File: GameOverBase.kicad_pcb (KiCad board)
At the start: 4 copper layers, 50 x 30 mm, 49 parts, among them J1 USB_C_DEALON-USB-US31-106, J2 Serial Port, J3 add-on conn, Q1 PMN48XP, SW1 SW_DIP_x08, SW2 boot, SW3 Reset, U1 ESP32-WROOM-E, U2 4021, U3 MCP73831-2ACI-OT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

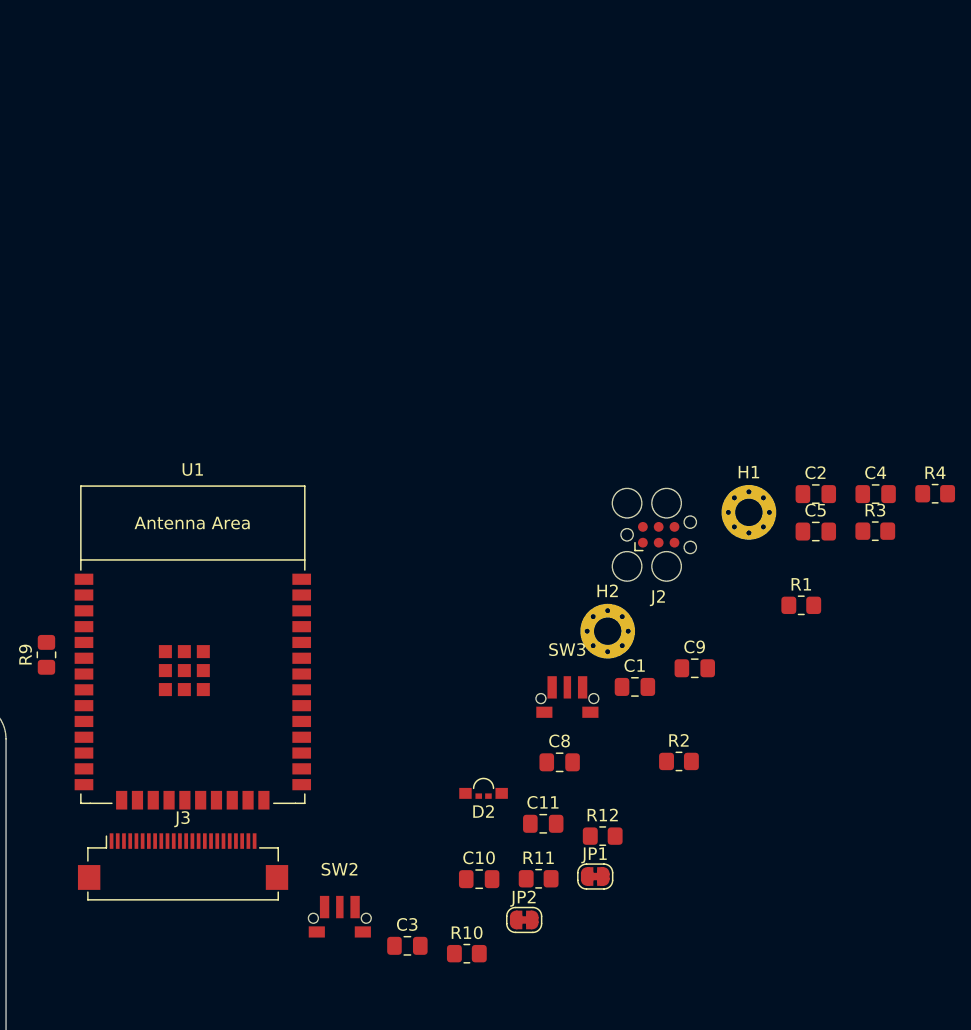
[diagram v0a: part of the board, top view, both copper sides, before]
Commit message: Groups ESP32 circuitry and add-on connector
To do this, I reorganized the order the GPIO pins are broken out to the
add-on connector.

This is still missing the decoupling capacitors on the connector
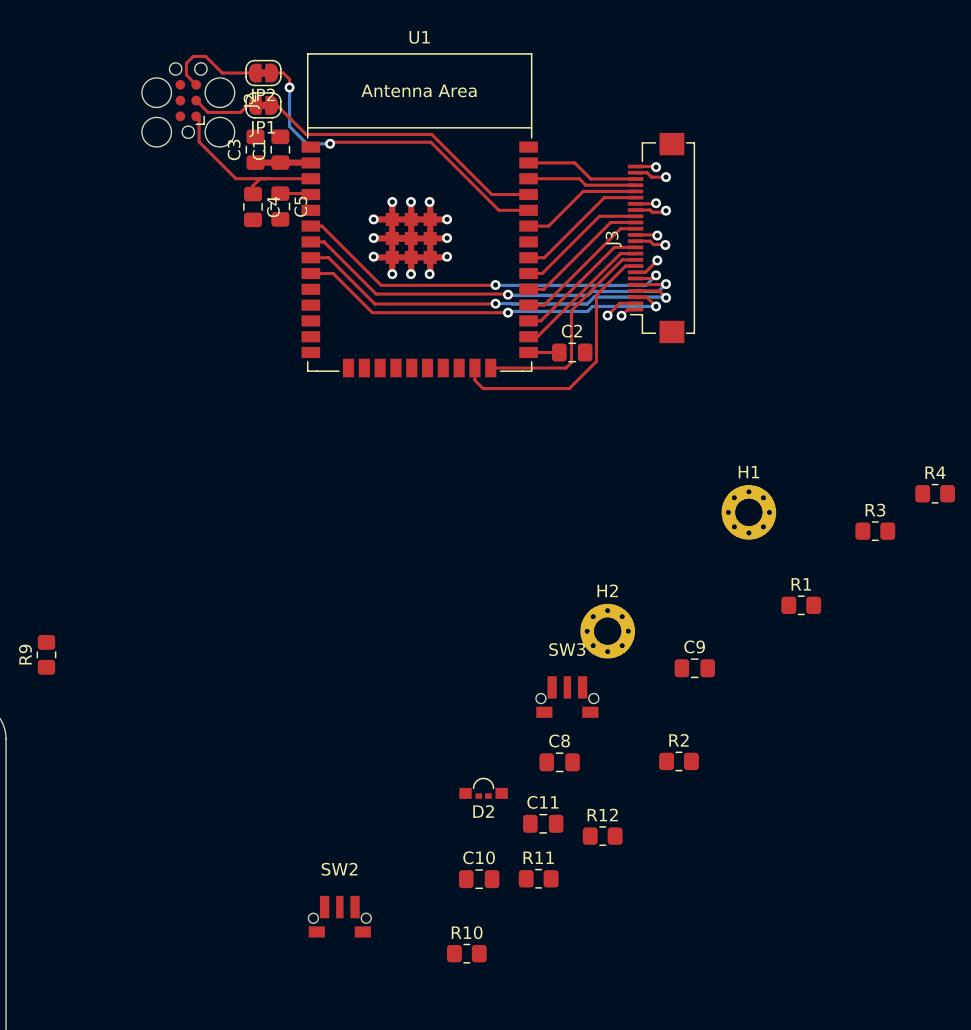
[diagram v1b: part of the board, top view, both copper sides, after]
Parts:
- moved JP2 71.2 mm to (190.7, 29.5), turned to 180 degrees
- moved JP1 67.5 mm to (190.7, 32.1), turned to 180 degrees
- moved C3 65.1 mm to (190.1, 35.6), turned to 90 degrees
- moved J3 63.2 mm to (222.4, 42.8), turned to 90 degrees
- moved C4 55.1 mm to (189.8, 40.2), turned to -90 degrees
- moved C1 51.7 mm to (192.1, 35.6), turned to 90 degrees
- moved J2 51.5 mm to (184.7, 31.7), turned to 90 degrees
- moved C5 50.3 mm to (192.1, 40.2), turned to -90 degrees
- moved U1 39.2 mm to (203.2, 42.5)
- moved C2 22.6 mm to (215.5, 52.0)
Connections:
- J3 pad 10: IO18 -> IO4
- J3 pad 11: IO19 -> IO16
- J3 pad 14: IO21 -> IO17
- J3 pad 15: IO22 -> IO5
- J3 pad 16: IO23 -> IO18
- J3 pad 19: IO32 -> IO19
- J3 pad 20: IO33 -> IO21
- J3 pad 21: IO34 -> IO22
- J3 pad 22: IO35 -> IO23
- J3 pad 3: IO2 -> IO33
- J3 pad 4: IO4 -> IO32
- J3 pad 5: IO5 -> IO35
- J3 pad 6: IO15 -> IO34
- J3 pad 8: IO16 -> IO15
- J3 pad 9: IO17 -> IO2
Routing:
- net GND: track 0.00 -> 46.7 mm, vias 0 -> 17
- net IO35: track 0.00 -> 33.2 mm, vias 0 -> 2
- net IO32: track 0.00 -> 33.1 mm, vias 0 -> 2
- net IO34: track 0.00 -> 31.8 mm, vias 0 -> 2
- net IO33: track 0.00 -> 31.2 mm, vias 0 -> 2
- net ESP_RX: track 0.00 -> 27.6 mm, vias 0 -> 2
- net ESP_TX: track 0.00 -> 23.6 mm
- net IO15: track 0.00 -> 21.4 mm
- net IO2: track 0.00 -> 17.7 mm
- net ESP_EN: track 0.00 -> 14.2 mm
- net +3V3: track 0.00 -> 13.5 mm, vias 0 -> 4
- net IO4: track 0.00 -> 11.4 mm
- net IO17: track 0.00 -> 11.1 mm
- net IO16: track 0.00 -> 11.0 mm
- net IO5: track 0.00 -> 10.8 mm
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
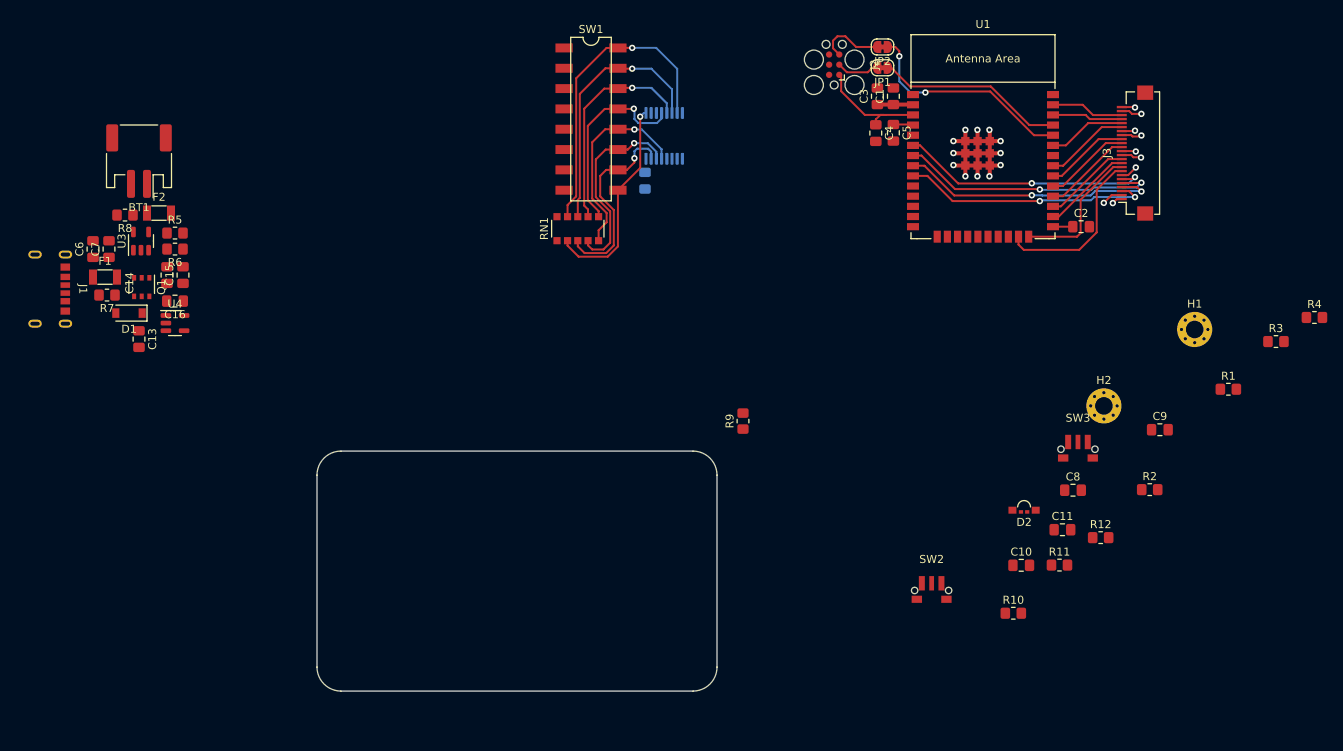
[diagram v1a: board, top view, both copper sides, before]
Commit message: Adds decoupling caps to the add-on connector and places the ESP on the pcb
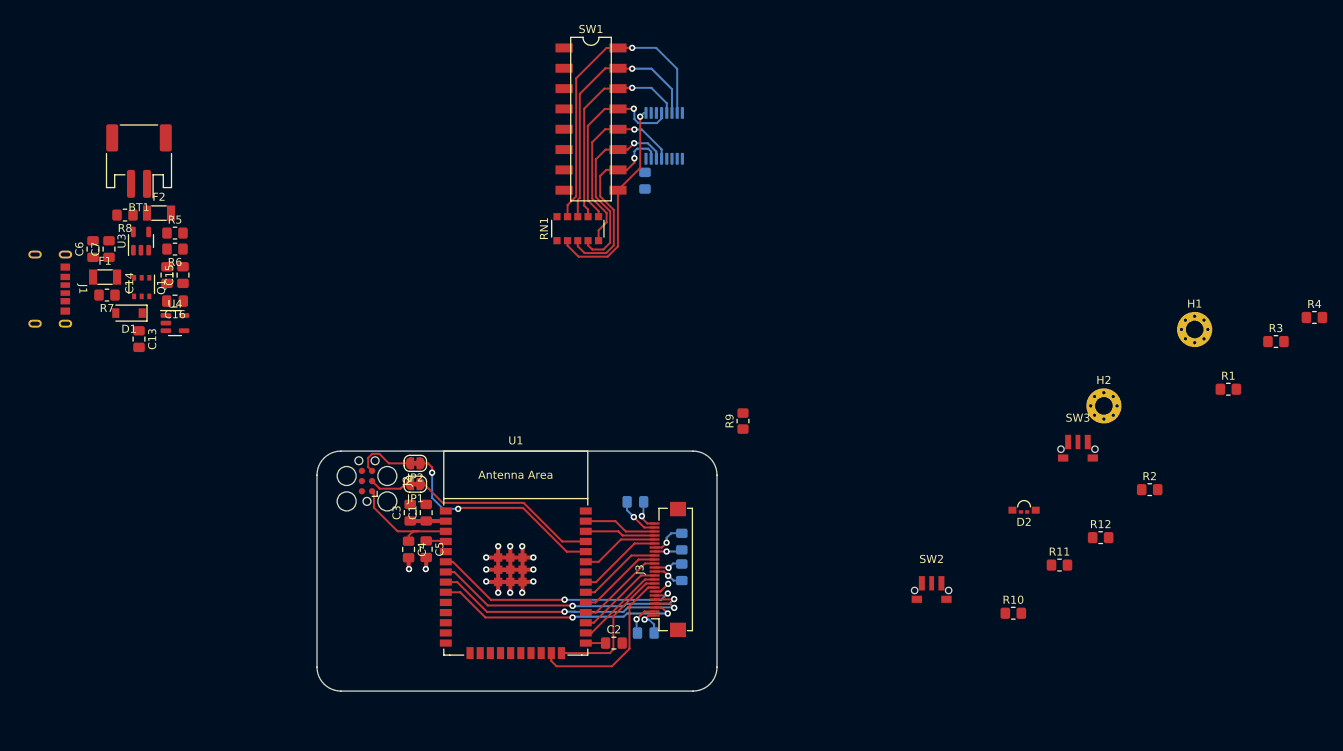
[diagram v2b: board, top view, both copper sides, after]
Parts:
- C10, C11, C8, C9: moved to B.Cu
- moved C1 78.2 mm to (133.7, 87.7)
- moved C3 78.2 mm to (131.7, 87.7)
- moved C4 78.2 mm to (131.4, 92.3)
- moved C5 78.2 mm to (133.7, 92.3)
- moved J2 78.2 mm to (126.2, 83.8)
- moved JP1 78.2 mm to (132.3, 84.1)
- moved JP2 78.2 mm to (132.3, 81.5)
- moved U1 78.2 mm to (144.8, 94.5)
- moved C2 78.2 mm to (157.1, 104.0)
- moved J3 78.2 mm to (164.1, 94.8)
- moved C9 69.1 mm to (161.1, 102.8), turned to 180 degrees
- moved C11 53.5 mm to (159.8, 86.3)
- moved C8 49.3 mm to (165.6, 91.3), turned to 90 degrees
- moved C10 42.4 mm to (165.6, 95.2), turned to 90 degrees
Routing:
- net GND: track 46.7 -> 58.3 mm, vias 17 -> 19
- net +3V3: track 13.5 -> 21.2 mm
- net Net-(J2-Pin_5): track 8.37 -> 7.78 mm

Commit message: Roughly routes buttons and RGB led
To make this routing better I also switched around the GPIO pins for the
RGB leds.
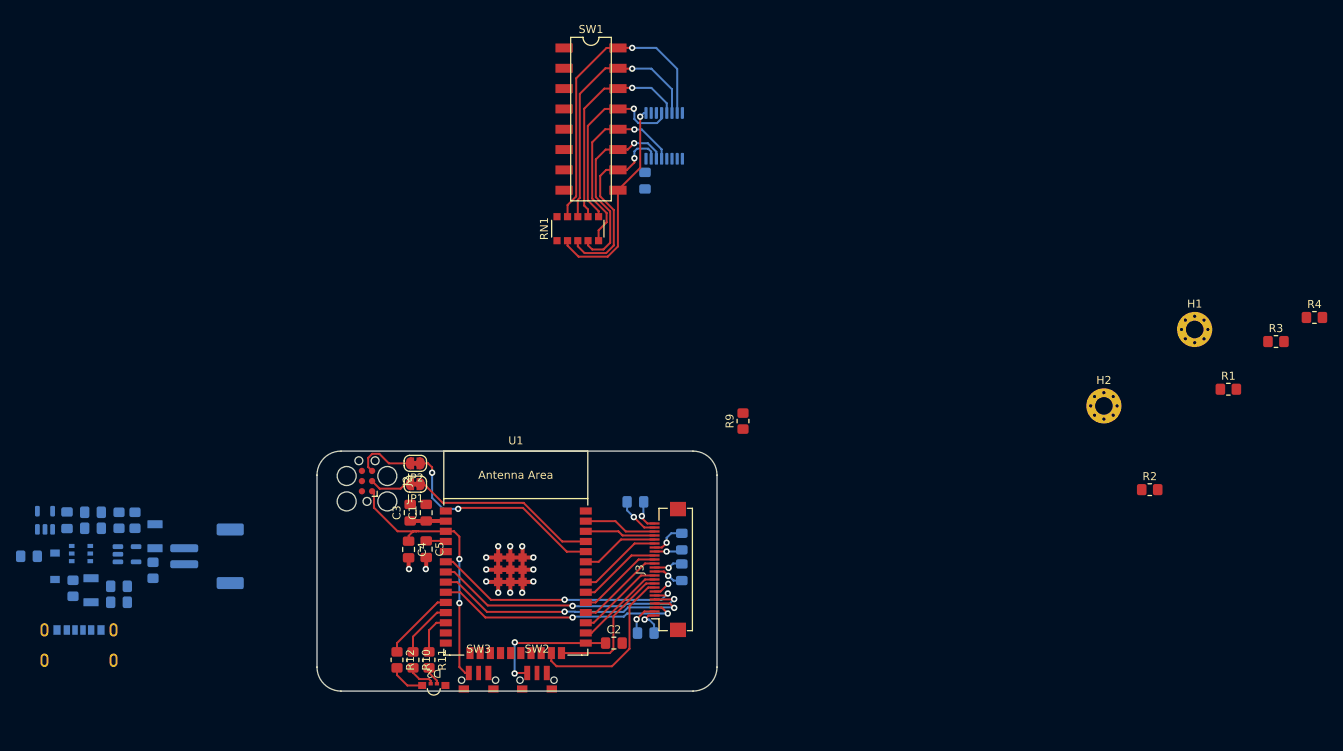
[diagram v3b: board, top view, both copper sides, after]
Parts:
- BT1, C13, C14, C15, C16, C6, C7, D1, F1, F2, J1, Q1, R5, R6, R7, R8, U3, U4: moved to B.Cu
- moved R12 89.3 mm to (130.0, 106.1), turned to -90 degrees
- moved SW3 80.3 mm to (140.2, 107.7)
- moved R11 79.7 mm to (134.0, 106.1), turned to -90 degrees
- moved D2 77.0 mm to (134.6, 109.3), turned to 180 degrees
- moved R10 75.3 mm to (132.0, 106.1), turned to -90 degrees
- moved SW2 50.6 mm to (147.5, 107.7)
- moved BT1 50.1 mm to (106.2, 93.2), turned to -90 degrees
- moved J1 45.6 mm to (90.2, 105.2), turned to 180 degrees
- moved R8 44.5 mm to (99.5, 94.9), turned to -90 degrees
- moved C6 44.3 mm to (95.2, 98.9), turned to 0 degrees
- moved C7 42.2 mm to (95.2, 96.9), turned to 0 degrees
- moved F2 40.4 mm to (99.8, 90.7), turned to 90 degrees
- moved F1 39.2 mm to (91.8, 97.4), turned to 90 degrees
- moved U3 39.2 mm to (96.2, 92.9), turned to 0 degrees
- moved R7 36.9 mm to (89.5, 97.2), turned to -90 degrees
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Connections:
- U1 pad 10: BAT_IND_R -> BAT_IND_B
- U1 pad 11: BAT_IND_G -> BAT_IND_R
- U1 pad 12: BAT_IND_B -> BAT_IND_G
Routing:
- net ESP_EN: track 14.2 -> 34.0 mm, vias 0 -> 2
- net ESP_BOOT: track 2.47 -> 16.9 mm, vias 0 -> 2
- net BAT_IND_B: track 0.00 -> 9.30 mm
- net BAT_IND_R: track 0.00 -> 7.25 mm
- net BAT_IND_G: track 0.00 -> 5.19 mm
- net Net-(D2-BK): track 0.00 -> 4.58 mm
- net Net-(D2-RK): track 0.00 -> 3.60 mm
- net Net-(D2-GK): track 0.00 -> 2.39 mm

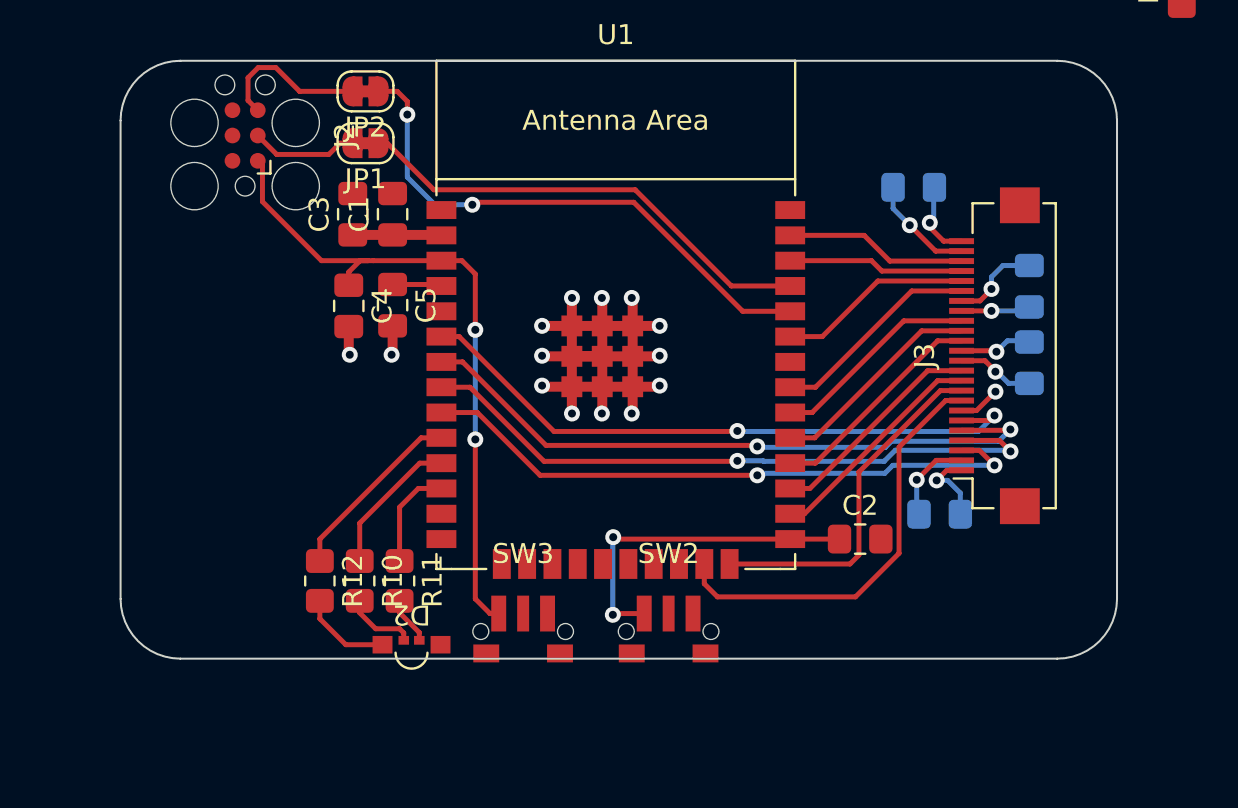
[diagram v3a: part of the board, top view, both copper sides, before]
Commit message: Increases board height to 3.5cm
This increases the overall size quite a bit, but gives us much more
space, which will be necessary for the DIP switches.
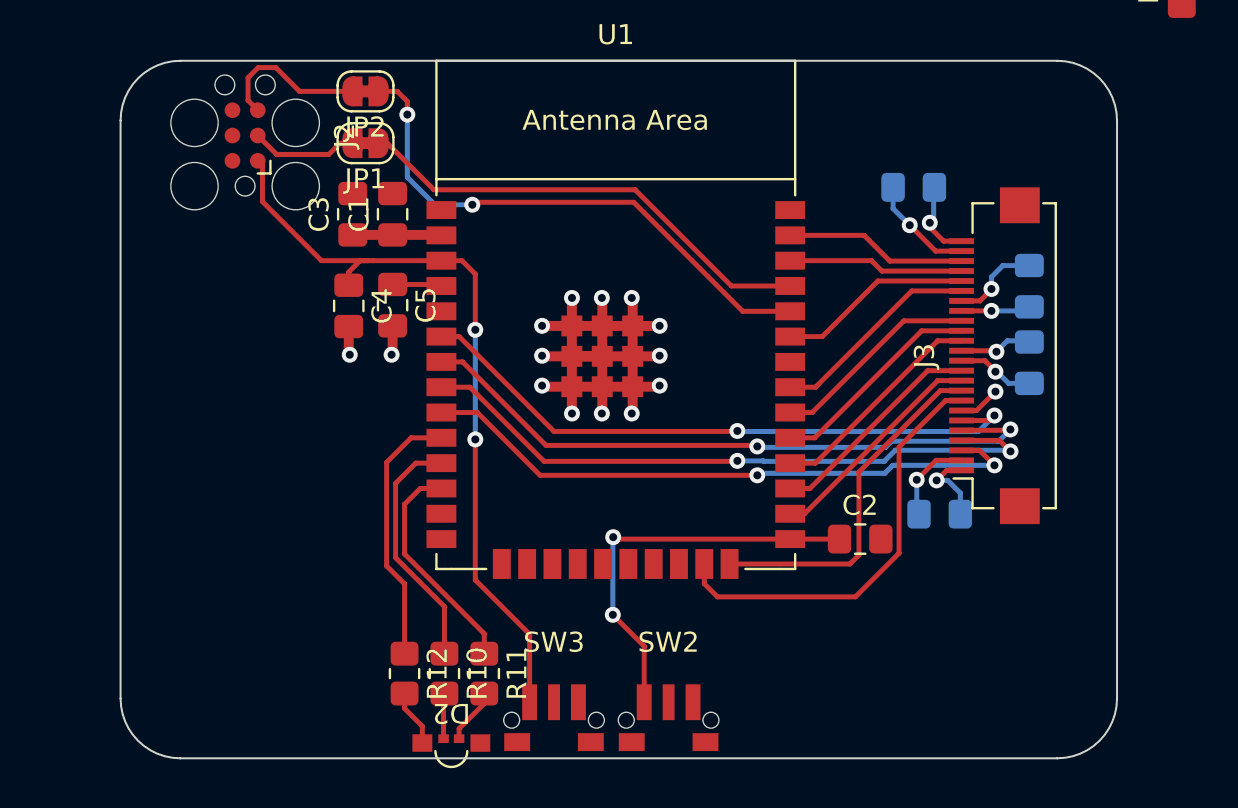
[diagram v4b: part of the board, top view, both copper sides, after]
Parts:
- moved R10 6.30 mm to (136.2, 110.8)
- moved R11 6.30 mm to (138.2, 110.8)
- moved R12 6.30 mm to (134.2, 110.8)
- moved D2 5.32 mm to (136.6, 114.2)
- moved SW3 4.71 mm to (141.8, 112.2)
- moved SW2 4.45 mm to (147.5, 112.2)
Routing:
- net BAT_IND_G: track 5.19 -> 11.3 mm
- net BAT_IND_R: track 7.25 -> 12.3 mm
- net ESP_EN: track 34.0 -> 38.8 mm
- net BAT_IND_B: track 9.30 -> 13.2 mm
- net ESP_BOOT: track 16.9 -> 20.3 mm
- net Net-(D2-BK): track 4.58 -> 2.85 mm
- net Net-(D2-RK): track 3.60 -> 2.28 mm
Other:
- board size 50 x 30 mm -> 50 x 35 mm
